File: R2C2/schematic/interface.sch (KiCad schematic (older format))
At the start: 4 parts, among them J18 R2C2, J20 R2C2, P3 AUX_IN, U1 LM7812

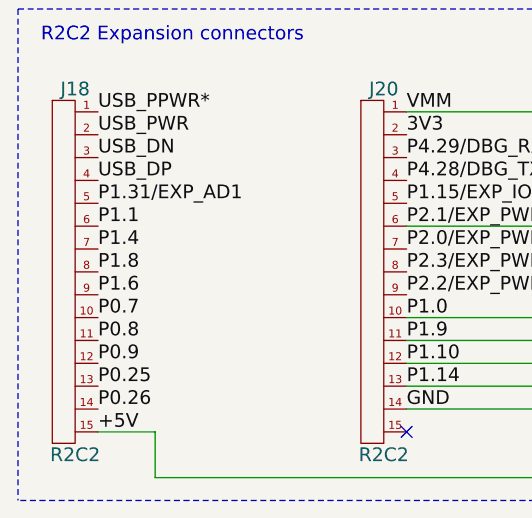
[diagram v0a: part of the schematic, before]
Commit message: Added nozzle test script. Still some unexpected nozzle patterns visible: E seems to be lagging X
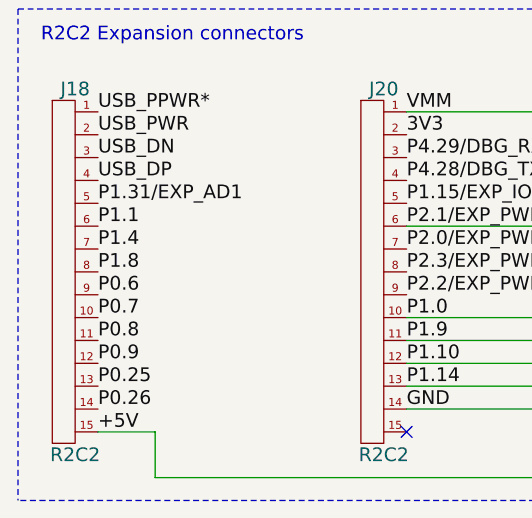
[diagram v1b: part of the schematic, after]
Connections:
- net labels added: P0.6
- net labels removed: P1.6
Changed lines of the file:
@@
-EESchema Schematic File Version 2  date 5/9/2013 1:19:29 PM
+EESchema Schematic File Version 2  date 5/9/2013 11:04:18 PM
 LIBS:power
 LIBS:device
@@
 P0.8
 Text Label 3600 3250 0    60   ~ 0
-P1.6
+P0.6
 Text Label 3600 3350 0    60   ~ 0
 P0.7
